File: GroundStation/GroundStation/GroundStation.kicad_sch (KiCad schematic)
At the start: 70 parts, among them J1 SD_Card_Receptacle, J4 Conn_Coaxial, J5 Conn_01x02, P1 USB_C_Plug_USB2.0, Q1 TSM3481CX6 RFG, U1 STM32F103C8Tx, U101 LD1117S33TR_SOT223, U2 E22-400T30S_LoRa, U4 TPS54538RQFR, U9 NEO-M9N-00B

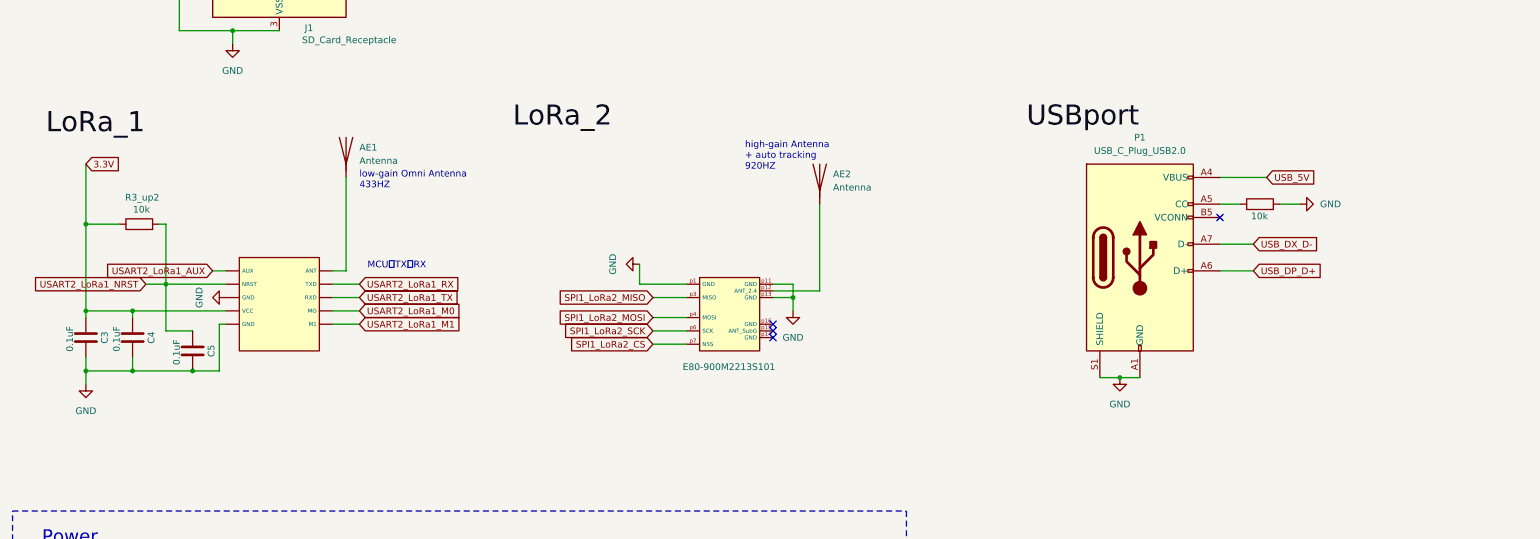
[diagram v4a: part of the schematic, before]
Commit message: Ray revise two LoRamodule, need Joyce help for free routing
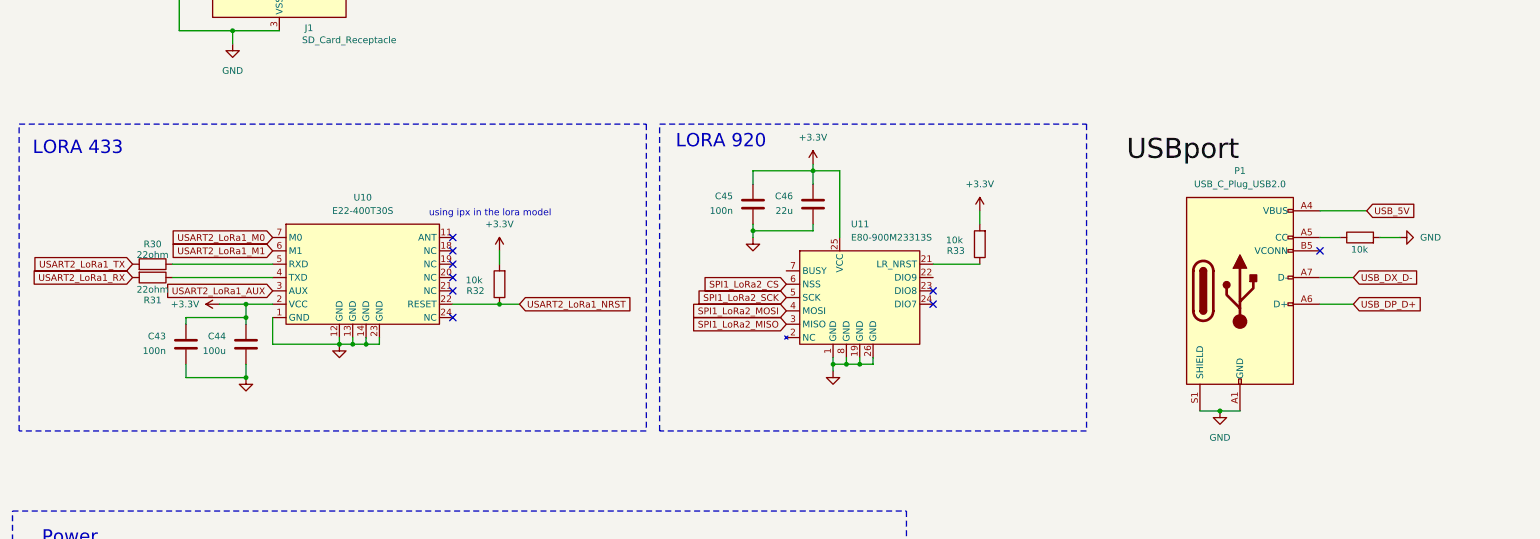
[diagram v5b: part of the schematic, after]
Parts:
- removed AE1, AE2: Antenna, Connector_Coaxial:SMA_Molex_73251-1153_EdgeMount_Horizontal, symbol Device:Antenna
- removed C3, C4, C5: 0.1uF, Capacitor_SMD:C_0805_2012Metric_Pad1.18x1.45mm_HandSolder, symbol Device:C
- removed E80-900M2213S101: ~, RF:E80-900M2213S, symbol LoRa2_E80-900M2213S:_1
- removed R3_up2: 10k, Resistor_SMD:R_0805_2012Metric_Pad1.20x1.40mm_HandSolder, symbol Device:R
- removed U2: E22-400T30S_LoRa, Library:e22-400t30s_Package, symbol E22-400T30S_new:E22-400T30S
- added C43, C45: 100n, Capacitor_SMD:C_0805_2012Metric_Pad1.18x1.45mm_HandSolder, symbol Device:C
- added C44: 100u, Capacitor_SMD:C_0805_2012Metric_Pad1.18x1.45mm_HandSolder, symbol Device:C
- added C46: 22u, Capacitor_SMD:C_0805_2012Metric_Pad1.18x1.45mm_HandSolder, symbol Device:C
- added R30, R31: 22ohm, Resistor_SMD:R_0805_2012Metric_Pad1.20x1.40mm_HandSolder, symbol Device:R
- added R32, R33: 10k, Resistor_SMD:R_0805_2012Metric_Pad1.20x1.40mm_HandSolder, symbol Device:R
- added U10: E22-400T30S, Library:e22-400t30s_Package, symbol A_library:E22-XXXT30
- added U11: E80-900M23313S, RF:E80-900M2213S, symbol A_library:E80-xxxM2213S
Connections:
- net +3.3V: now also C43.1, C44.1, C45.1, C46.1, R32.2, R33.2, U10.2 (VCC), U11.25 (VCC)
- net GND: now also C43.2, C44.2, C45.2, C46.2, U10.1 (GND), U10.12 (GND), U10.13 (GND), U10.14 (GND), U10.23 (GND), U11.1 (GND), U11.19 (GND), U11.26 (GND), U11.8 (GND)
- net SPI1_LoRa2_CS: now also U11.6 (NSS)
- net SPI1_LoRa2_MISO: now also U11.3 (MISO)
- net SPI1_LoRa2_MOSI: now also U11.4 (MOSI)
- net SPI1_LoRa2_SCK: now also U11.5 (SCK)
- net USART2_LoRa1_AUX: now also U10.3 (AUX)
- net USART2_LoRa1_M0: now also U10.7 (M0)
- net USART2_LoRa1_M1: now also U10.6 (M1)
- net USART2_LoRa1_NRST: now also R32.1, U10.22 (RESET)
- net USART2_LoRa1_RX: now also R31.2
- net USART2_LoRa1_TX: now also R30.2
- new net: R31.1, U10.4 (TXD)
- new net: R33.1, U11.21 (LR_NRST)
- new net: R30.1, U10.5 (RXD)
- no-connect marks 42 -> 47
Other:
- note added: "LORA 433"
- note added: "LORA 920"
- note added: "using ipx in the lora model"
- note removed: "high-gain Antenna + auto tracking 920HZ"
- note removed: "low-gain Omni Antenna 433HZ"
- moved on the sheet: P1
